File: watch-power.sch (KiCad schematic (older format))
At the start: 21 parts, among them IC1 BQ24230, IC2 LC709203FQH-01TWG, IC3 DRV2603RUNR, IC4 TPS63030, J1 47346-0001, J2 1-1734592-4, M1 Vibramotor

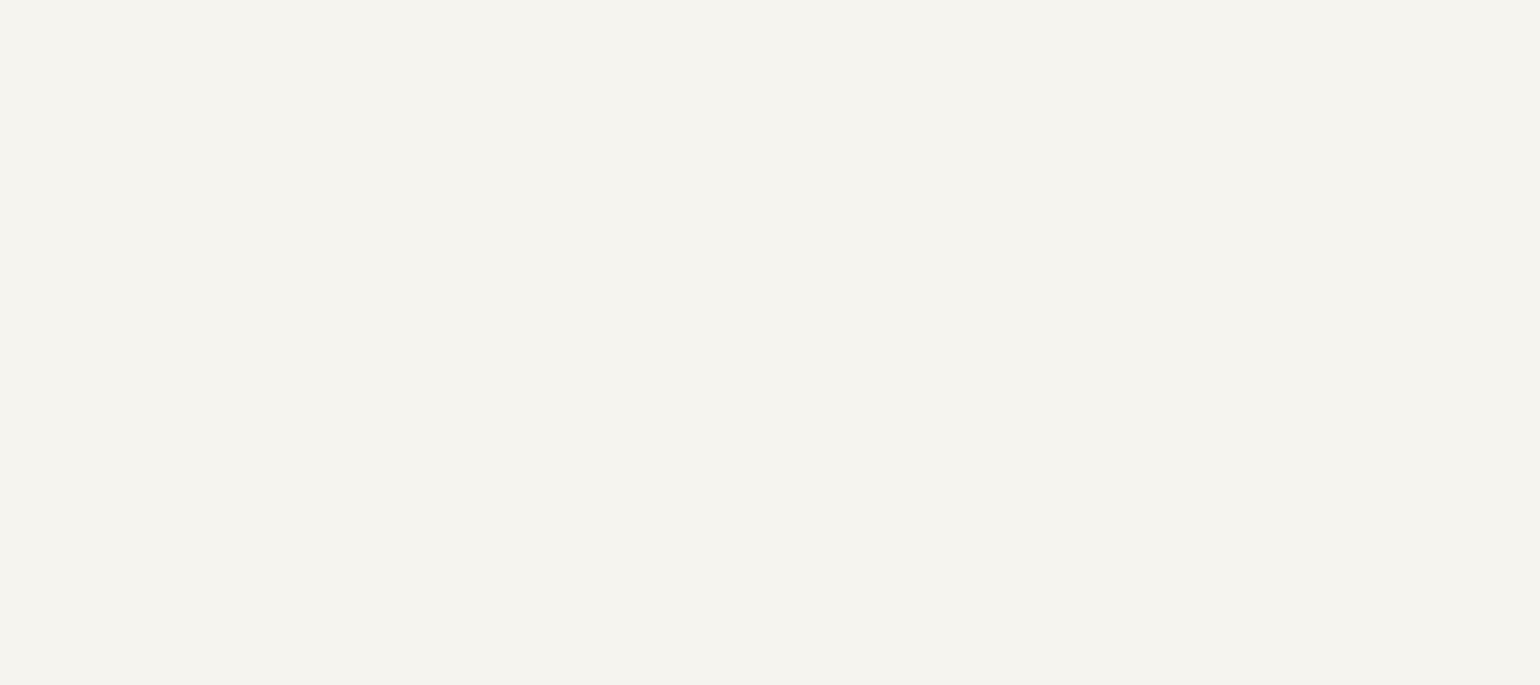
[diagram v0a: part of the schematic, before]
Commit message: add some schematic parts around nrf52
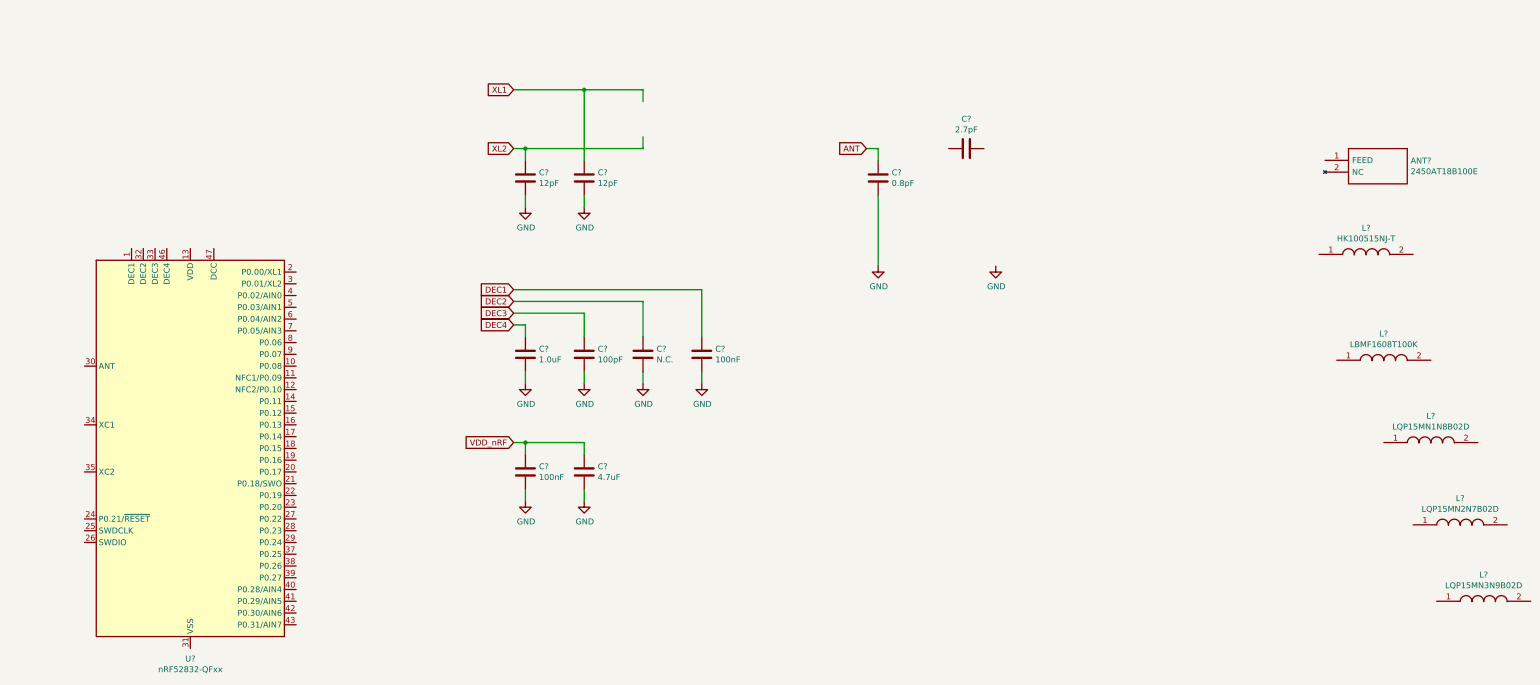
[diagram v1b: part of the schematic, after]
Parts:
- added ANT?: 2450AT18B100E, ANTC3216X140N, symbol 2450AT18B100E:2450AT18B100E
- added C?: 1.0uF, symbol Device:C
- added C?: 100pF, symbol Device:C
- added C?: N.C., symbol Device:C
- added C? (x2): 100nF, symbol Device:C
- added C?: 4.7uF, symbol Device:C
- added C? (x2): 12pF, symbol Device:C
- added C?: 0.8pF, symbol Device:C
- added C?: 2.7pF, symbol Device:C
- added L?: HK100515NJ-T, INDC1005X55N, symbol HK100515NJ-T:HK100515NJ-T
- added L?: LBMF1608T100K, INDC1608X100N, symbol LBMF1608T100K:LBMF1608T100K
- added L?: LQP15MN1N8B02D, LQP15MN10NG02D, symbol LQP15MN1N8B02D:LQP15MN1N8B02D
- added L?: LQP15MN2N7B02D, LQP15MN10NG02D, symbol LQP15MN2N7B02D:LQP15MN2N7B02D
- added L?: LQP15MN3N9B02D, LQP15MN10NG02D, symbol LQP15MN3N9B02D:LQP15MN3N9B02D
- added U?: nRF52832-QFxx, Package_DFN_QFN:QFN-48-1EP_6x6mm_P0.4mm_EP4.6x4.6mm, symbol MCU_Nordic:nRF52832-QFxx
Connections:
- net labels added: ANT, DEC1, DEC2, DEC3, DEC4, GND, VDD_nRF, XL1, XL2
- wire segments 0 -> 31

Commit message: big save
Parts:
- removed C?: 1.0uF, symbol Device:C
- removed IC1: BQ24230, BQ24230RGTR:QFN50P300X300X100-17N-D, symbol BQ24230RGTR:BQ24230
- removed IC2: LC709203FQH-01TWG, SON65P400X300X80-9N, symbol LC709203FQH-01TWG:LC709203FQH-01TWG
- removed IC3: DRV2603RUNR, QFN50P200X200X80-10N-D, symbol DRV2603RUNR:DRV2603RUNR
- removed IC4: TPS63030, TPS63030DSKR:SON50P250X250X80-11N-D, symbol TPS63030DSKR:TPS63030
- added AC1: LSM6DSOXTR, LSM6DSOXTR:LGA-14_1, symbol LSM6DSOXTR:LSM6DSOXTR
- added AE1: Antenna, symbol Device:Antenna
- added BZ1: Buzzer, symbol Device:Buzzer
- added C10: 1.0uF, Capacitor_SMD:C_0603_1608Metric, symbol Device:C
- added C18, C19, C25: 100nF, symbol Device:C
- added C20: C, symbol Device:C
- added C21, C22, C27: 1uF, symbol Device:C
- added C23, C24: 12pF, Capacitor_SMD:C_0402_1005Metric, symbol Device:C
- added C26: 10uF, symbol Device:C
- added IC1: TPS63030, symbol TPS63030DSKR:TPS63030
- added IC2: MMBT2222ALT1G, SOT96P237X111-3N, symbol MMBT2222ALT1G:MMBT2222ALT1G
- added IC3: BQ24230, symbol BQ24230RGTR:BQ24230
- added IC4: DRV2603RUNR, symbol DRV2603RUNR:DRV2603RUNR
- added IC5: LC709203F, symbol LC709203FQH-01TWG:LC709203F
- added J3: Battery, symbol Connector_Generic:Conn_01x02
- added Q1: 2N2219, Package_TO_SOT_THT:TO-39-3, symbol Transistor_BJT:2N2219
- added R10: 1k, symbol Device:R
- added R11, R12, R13, R14, R15, R16, R7: 10k, symbol Device:R
- added R6: 22R, symbol Device:R
- added R8, R9: 100k, Resistor_SMD:R_0603_1608Metric, symbol Device:R
- added U2: APDS9960, APDS-9960:APDS-9950, symbol APDS-9960:APDS9960
- added U3: ST7735, ST7735:ST7735_curved, symbol ST7735:ST7735
- C11, C12, C13, C14, C17, C8, C9: renamed from C?; footprint (none) -> Capacitor_SMD:C_0402_1005Metric
- C15: renamed from C?; footprint (none) -> Capacitor_SMD:C_0603_1608Metric
- M1: footprint Vibramotor:Vibramotor -> (none)
- gave numbers to parts that had none: 8
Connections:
- net labels added: +3V3, BATT_M, BATT_P, CHARGER_CE, CHARGER_CHG, CHARGER_EN1, CHARGER_EN2, CHARGER_PGOOD, CHARGER_TD, DCDC, DISPLAY_BACKLIGHT, DISPLAY_CS, DISPLAY_DC, DISPLAY_MOSI, DISPLAY_RESET, DISPLAY_SCK, FUEL_GAUGE_ALARMB, FUEL_GAUGE_SCL, FUEL_GAUGE_SDA, GESTURE_INT, GESTURE_SCL, GESTURE_SDA, IMU_CS, IMU_INT1, IMU_INT2, IMU_MISO, IMU_MOSI, IMU_SCK, LEDK, SWDCLK, SWDIO, VIBRAMOTOR_EN, VIBRAMOTOR_PWM, XC1, XC2, ~RESET
- wire segments 31 -> 255
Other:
- note added: "- ep és vss összekötése?\n- 2 bat és 2 out jó?\n- usb-re szebb szimbólum?\n- alsó 3 tényleg úgy van?\n- összeszedni mi kell valójában az MCU felé\n"
- note added: "BATTERY vagy 3v3?"
- note added: "TMR: vagy föld vagy ellenállás és föld"
- note added: "legyen ilyen a buzzerem\ncsak sárga"
- note added: "legyen szélesebb a szimbólum\n"
- moved on the sheet: ANT1, C1, C11, C12, C13, C14, C15, C16, C17, C2, C3, C4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

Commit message: save
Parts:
- removed Q1: 2N2219, Package_TO_SOT_THT:TO-39-3, symbol Transistor_BJT:2N2219
- added R17: 100R, Resistor_SMD:R_0402_1005Metric, symbol Device:R
- C18, C19, C21, C22, C25: footprint (none) -> Capacitor_SMD:C_0402_1005Metric
- C20: value C -> 0.1uF; footprint (none) -> Capacitor_SMD:C_0201_0603Metric
- R10, R11, R13, R15, R6, R7: footprint (none) -> Resistor_SMD:R_0402_1005Metric
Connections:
- net +3V3: now also C25.1, R11.1; no longer C26.1
- net DISPLAY_BACKLIGHT: now also R11.2
- net GND: now also C25.2, IC2.2 (E); no longer C26.2, R11.2
- net at IC2.1 (B): now also R10.1
- net at IC2.3 (C): now also R17.2
- net LEDK: no longer names the net of U3.11 (LEDK)
- net LEDK: now also R17.1
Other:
- note added: "ehelyett kell a bulk storage"
- moved on the sheet: C25, C26, IC2, R10, R11
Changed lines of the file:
@@
 P 12500 1750
 F 0 "C20" H 12615 1796 50  0000 L CNN
-F 1 "C" H 12615 1705 50  0000 L CNN
-F 2 "" H 12538 1600 50  0001 C CNN
+F 1 "0.1uF" H 12615 1705 50  0000 L CNN
+F 2 "Capacitor_SMD:C_0201_0603Metric" H 12538 1600 50  0001 C CNN
 F 3 "~" H 12500 1750 50  0001 C CNN
 	1    12500 1750
@@
 F 0 "R7" H 18070 1796 50  0000 L CNN
 F 1 "10k" H 18070 1705 50  0000 L CNN
-F 2 "" V 17930 1750 50  0001 C CNN
+F 2 "Resistor_SMD:R_0402_1005Metric" V 17930 1750 50  0001 C CNN
 F 3 "~" H 18000 1750 50  0001 C CNN
 	1    18000 1750
@@
 F 0 "C22" H 16615 1896 50  0000 L CNN
 F 1 "1uF" H 16615 1805 50  0000 L CNN
-F 2 "" H 16538 1700 50  0001 C CNN
+F 2 "Capacitor_SMD:C_0402_1005Metric" H 16538 1700 50  0001 C CNN
 F 3 "~" H 16500 1850 50  0001 C CNN
 	1    16500 1850
@@
 F 0 "R6" V 16043 1600 50  0000 C CNN
 F 1 "22R" V 16134 1600 50  0000 C CNN
-F 2 "" V 16180 1600 50  0001 C CNN
+F 2 "Resistor_SMD:R_0402_1005Metric" V 16180 1600 50  0001 C CNN
 F 3 "~" H 16250 1600 50  0001 C CNN
 	1    16250 1600
@@
 F 0 "C21" H 16115 2796 50  0000 L CNN
 F 1 "1uF" H 16115 2705 50  0000 L CNN
-F 2 "" H 16038 2600 50  0001 C CNN
+F 2 "Capacitor_SMD:C_0402_1005Metric" H 16038 2600 50  0001 C CNN
 F 3 "~" H 16000 2750 50  0001 C CNN
 	1    16000 2750
@@
 F 0 "C18" H 11465 5446 50  0000 L CNN
 F 1 "100nF" H 11465 5355 50  0000 L CNN
-F 2 "" H 11388 5250 50  0001 C CNN
+F 2 "Capacitor_SMD:C_0402_1005Metric" H 11388 5250 50  0001 C CNN
 F 3 "~" H 11350 5400 50  0001 C CNN
 	1    11350 5400
@@
 F 0 "C19" H 12115 5446 50  0000 L CNN
 F 1 "100nF" H 12115 5355 50  0000 L CNN
-F 2 "" H 12038 5250 50  0001 C CNN
+F 2 "Capacitor_SMD:C_0402_1005Metric" H 12038 5250 50  0001 C CNN
 F 3 "~" H 12000 5400 50  0001 C CNN
 	1    12000 5400
@@
 L MMBT2222ALT1G:MMBT2222ALT1G IC2
 U 1 1 5F6541A0
-P 13950 10500
-F 0 "IC2" H 14350 10765 50  0000 C CNN
-F 1 "MMBT2222ALT1G" H 14350 10674 50  0000 C CNN
-F 2 "SOT96P237X111-3N" H 14600 10600 50  0001 L CNN
-F 3 "http://www.onsemi.com/pub/Collateral/MMBT2222LT1-D.PDF" H 14600 10500 50  0001 L CNN
-F 4 "MMBT2222ALT1G, NPN Bipolar Transistor,  0.6 A 40 V HFE:35 300 MHz Small Signal, 3-Pin SOT-23" H 14600 10400 50  0001 L CNN "Description"
-F 5 "1.11" H 14600 10300 50  0001 L CNN "Height"
-F 6 "863-MMBT2222ALT1G" H 14600 10200 50  0001 L CNN "Mouser Part Number"
-F 7 "https://www.mouser.co.uk/ProductDetail/ON-Semiconductor/MMBT2222ALT1G?qs=HVbQlW5zcXWwnD7Jokybqg%3D%3D" H 14600 10100 50  0001 L CNN "Mouser Price/Stock"
-F 8 "ON Semiconductor" H 14600 10000 50  0001 L CNN "Manufacturer_Name"
-F 9 "MMBT2222ALT1G" H 14600 9900 50  0001 L CNN "Manufacturer_Part_Number"
-	1    13950 10500
+P 14600 11600
+F 0 "IC2" H 15000 11865 50  0000 C CNN
+F 1 "MMBT2222ALT1G" H 15000 11774 50  0000 C CNN
+F 2 "SOT96P237X111-3N" H 15250 11700 50  0001 L CNN
+F 3 "http://www.onsemi.com/pub/Collateral/MMBT2222LT1-D.PDF" H 15250 11600 50  0001 L CNN
+F 4 "MMBT2222ALT1G, NPN Bipolar Transistor,  0.6 A 40 V HFE:35 300 MHz Small Signal, 3-Pin SOT-23" H 15250 11500 50  0001 L CNN "Description"
+F 5 "1.11" H 15250 11400 50  0001 L CNN "Height"
+F 6 "863-MMBT2222ALT1G" H 15250 11300 50  0001 L CNN "Mouser Part Number"
+F 7 "https://www.mouser.co.uk/ProductDetail/ON-Semiconductor/MMBT2222ALT1G?qs=HVbQlW5zcXWwnD7Jokybqg%3D%3D" H 15250 11200 50  0001 L CNN "Mouser Price/Stock"
+F 8 "ON Semiconductor" H 15250 11100 50  0001 L CNN "Manufacturer_Name"
+F 9 "MMBT2222ALT1G" H 15250 11000 50  0001 L CNN "Manufacturer_Part_Number"
+	1    14600 11600
 	1    0    0    -1
 $EndComp
@@
 L Device:R R11
 U 1 1 5F654DFC
-P 14500 11750
-F 0 "R11" H 14570 11796 50  0000 L CNN
-F 1 "10k" H 14570 11705 50  0000 L CNN
-F 2 "" V 14430 11750 50  0001 C CNN
-F 3 "~" H 14500 11750 50  0001 C CNN
-	1    14500 11750
+P 14000 11250
+F 0 "R11" H 14070 11296 50  0000 L CNN
+F 1 "10k" H 14070 11205 50  0000 L CNN
+F 2 "Resistor_SMD:R_0402_1005Metric" V 13930 11250 50  0001 C CNN
+F 3 "~" H 14000 11250 50  0001 C CNN
+	1    14000 11250
 	1    0    0    -1
 $EndComp
@@
 L Device:R R10
 U 1 1 5F655ABF
-P 14250 11500
-F 0 "R10" H 14320 11546 50  0000 L CNN
-F 1 "1k" H 14320 11455 50  0000 L CNN
-F 2 "" V 14180 11500 50  0001 C CNN
-F 3 "~" H 14250 11500 50  0001 C CNN
-	1    14250 11500
+P 14250 11600
+F 0 "R10" H 14320 11646 50  0000 L CNN
+F 1 "1k" H 14320 11555 50  0000 L CNN
+F 2 "Resistor_SMD:R_0402_1005Metric" V 14180 11600 50  0001 C CNN
+F 3 "~" H 14250 11600 50  0001 C CNN
+	1    14250 11600
 	0    1    1    0
 $EndComp
@@
 L Device:C C26
 U 1 1 5F730623
-P 15500 2250
-F 0 "C26" H 15615 2296 50  0000 L CNN
-F 1 "10uF" H 15615 2205 50  0000 L CNN
-F 2 "" H 15538 2100 50  0001 C CNN
-F 3 "~" H 15500 2250 50  0001 C CNN
-	1    15500 2250
+P 15150 2200
+F 0 "C26" H 15265 2246 50  0000 L CNN
+F 1 "10uF" H 15265 2155 50  0000 L CNN
+F 2 "" H 15188 2050 50  0001 C CNN
+F 3 "~" H 15150 2200 50  0001 C CNN
+	1    15150 2200
 	1    0    0    -1
 $EndComp
@@
 F 0 "R13" H 18570 1796 50  0000 L CNN
 F 1 "10k" H 18570 1705 50  0000 L CNN
-F 2 "" V 18430 1750 50  0001 C CNN
+F 2 "Resistor_SMD:R_0402_1005Metric" V 18430 1750 50  0001 C CNN
 F 3 "~" H 18500 1750 50  0001 C CNN
 	1    18500 1750
@@
 F 0 "R15" H 19070 1796 50  0000 L CNN
 F 1 "10k" H 19070 1705 50  0000 L CNN
-F 2 "" V 18930 1750 50  0001 C CNN
+F 2 "Resistor_SMD:R_0402_1005Metric" V 18930 1750 50  0001 C CNN
 F 3 "~" H 19000 1750 50  0001 C CNN
 	1    19000 1750
@@
 Wire Wire Line
 	6300 4800 5300 4800
-$Comp
-L Transistor_BJT:2N2219 Q1
-U 1 1 5F92B3C0
-P 14900 11500
-F 0 "Q1" H 15090 11546 50  0000 L CNN
-F 1 "2N2219" H 15090 11455 50  0000 L CNN
-F 2 "Package_TO_SOT_THT:TO-39-3" H 15100 11425 50  0001 L CIN
-F 3 "http://www.onsemi.com/pub_link/Collateral/2N2219-D.PDF" H 14900 11500 50  0001 L CNN
-	1    14900 11500
-	1    0    0    -1
-$EndComp
 Text GLabel 16200 10000 0    50   Input ~ 0
 DISPLAY_MOSI
@@
 L power:GND #PWR0161
 U 1 1 5FA1AB75
-P 15000 12100
-F 0 "#PWR0161" H 15000 11850 50  0001 C CNN
-F 1 "GND" H 15005 11927 50  0000 C CNN
-F 2 "" H 15000 12100 50  0001 C CNN
-F 3 "" H 15000 12100 50  0001 C CNN
-	1    15000 12100
-	1    0    0    -1
-$EndComp
-Text GLabel 16200 11600 0    50   Input ~ 0
-LEDK
-Wire Wire Line
-	16300 11400 16300 11800
-Wire Wire Line
-	16300 11800 16500 11800
-Connection ~ 16300 11400
-Wire Wire Line
-	16500 11600 16200 11600
-Text GLabel 13900 11500 0    50   Input ~ 0
-DISPLAY_BACKLIGHT
-Text GLabel 15100 11000 2    50   Input ~ 0
-LEDK
-Wire Wire Line
-	13900 11500 14100 11500
-Wire Wire Line
-	14400 11500 14500 11500
-Wire Wire Line
-	14500 11500 14500 11600
-$Comp
-L power:GND #PWR0162
-U 1 1 5FA71E5D
 P 14500 12100
-F 0 "#PWR0162" H 14500 11850 50  0001 C CNN
+F 0 "#PWR0161" H 14500 11850 50  0001 C CNN
 F 1 "GND" H 14505 11927 50  0000 C CNN
 F 2 "" H 14500 12100 50  0001 C CNN
@@
 $EndComp
 Wire Wire Line
-	14500 12100 14500 11900
+	16300 11400 16300 11800
+Wire Wire Line
+	16300 11800 16500 11800
+Connection ~ 16300 11400
+Text GLabel 13900 11600 0    50   Input ~ 0
+DISPLAY_BACKLIGHT
 $Comp
 L Device:C C25
 U 1 1 5FA80791
-P 13400 10750
-F 0 "C25" H 13515 10796 50  0000 L CNN
-F 1 "100nF" H 13515 10705 50  0000 L CNN
-F 2 "" H 13438 10600 50  0001 C CNN
-F 3 "~" H 13400 10750 50  0001 C CNN
-	1    13400 10750
+P 17500 9750
+F 0 "C25" H 17615 9796 50  0000 L CNN
+F 1 "100nF" H 17615 9705 50  0000 L CNN
+F 2 "Capacitor_SMD:C_0402_1005Metric" H 17538 9600 50  0001 C CNN
+F 3 "~" H 17500 9750 50  0001 C CNN
+	1    17500 9750
 	1    0    0    -1
 $EndComp
@@
 Text GLabel 9400 14500 0    50   Input ~ 0
 DCDC
+Wire Wire Line
+	14400 11600 14600 11600
+Wire Wire Line
+	14100 11600 14000 11600
+Wire Wire Line
+	13900 11600 14000 11600
+Connection ~ 14000 11600
+$Comp
+L power:+3V3 #PWR0162
+U 1 1 5F83162B
+P 14000 11000
+F 0 "#PWR0162" H 14000 10850 50  0001 C CNN
+F 1 "+3V3" H 14015 11173 50  0000 C CNN
+F 2 "" H 14000 11000 50  0001 C CNN
+F 3 "" H 14000 11000 50  0001 C CNN
+	1    14000 11000
+	1    0    0    -1
+$EndComp
+Wire Wire Line
+	14500 12100 14500 11700
+Wire Wire Line
+	14500 11700 14600 11700
+$Comp
+L Device:R R17
+U 1 1 5F844A83
+P 15750 11600
+F 0 "R17" H 15820 11646 50  0000 L CNN
+F 1 "100R" H 15820 11555 50  0000 L CNN
+F 2 "Resistor_SMD:R_0402_1005Metric" V 15680 11600 50  0001 C CNN
+F 3 "~" H 15750 11600 50  0001 C CNN
+	1    15750 11600
+	0    1    1    0
+$EndComp
+Wire Wire Line
+	15400 11600 15600 11600
+Wire Wire Line
+	15900 11600 16500 11600
+Wire Wire Line
+	14000 11100 14000 11000
+Wire Wire Line
+	14000 11400 14000 11600
+$Comp
+L power:+3V3 #PWR0165
+U 1 1 5F8EA840
+P 17500 9500
+F 0 "#PWR0165" H 17500 9350 50  0001 C CNN
+F 1 "+3V3" H 17515 9673 50  0000 C CNN
+F 2 "" H 17500 9500 50  0001 C CNN
+F 3 "" H 17500 9500 50  0001 C CNN
+	1    17500 9500
+	1    0    0    -1
+$EndComp
+$Comp
+L power:GND #PWR0166
+U 1 1 5F8EAD7A
+P 17500 10000
+F 0 "#PWR0166" H 17500 9750 50  0001 C CNN
+F 1 "GND" H 17505 9827 50  0000 C CNN
+F 2 "" H 17500 10000 50  0001 C CNN
+F 3 "" H 17500 10000 50  0001 C CNN
+	1    17500 10000
+	1    0    0    -1
+$EndComp
+Wire Wire Line
+	17500 9600 17500 9500
+Wire Wire Line
+	17500 10000 17500 9900
+Text Notes 14650 2350 0    50   ~ 0
+ehelyett kell a bulk storage
 $EndSCHEMATC
